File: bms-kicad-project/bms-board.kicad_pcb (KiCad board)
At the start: 2 copper layers, 49 parts, among them J1 S7B-XH-A, Q1 BSS308PE_H6327, Q2 BSS308PE_H6327, Q3 BSS308PE_H6327, Q5 BSS308PE_H6327, Q6 BSS308PE_H6327, Q7 BSS308PE_H6327, U1 LTC6804-2

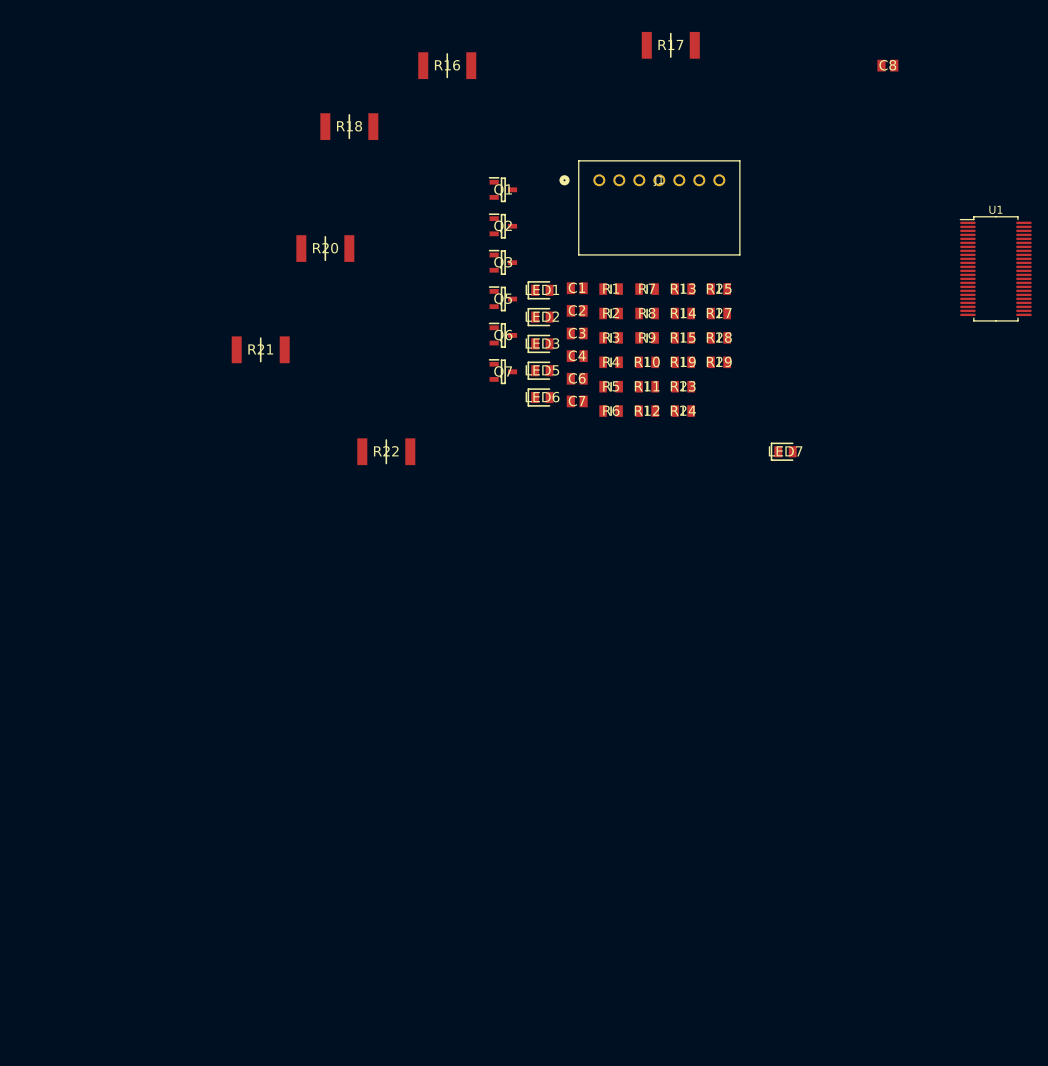
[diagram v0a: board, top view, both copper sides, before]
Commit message: Feature: Added schematic and symbols for 5V switching regulator (#16)
* feat: initial 5V-reg-and-edits branch commit

* feat: small to-do list edits

* feat: put filtering and balancing circuits into hierarchical format

* feat: forgot to commit smol change

* feat: Added SiC461 Schematic, Footprint, and 3D Model

* feat: Added all components listed in the spreadsheet, until Inductor L1

* feat: forgor the description

* feat: Added all symbols and 3D models. Also began working on Regulator Schematic.

* feat: Added more connections to the 5V Regulator schematic.

* feat: Added VFB connection in 5V Regulator Schematic

* feat: Added 220uf cap & modified 5V Reg Circuit

* feat: Added more to 5V Regulator Schematic

* feat: Changed all resistor symbols to be the standard KiCAD symbol, started improving schematic.

* feat: Forgot to save changes to schematic.

* feat: Just about completed 5V Regulator Schematic.

* feat: cosmetic changes to 5V reg schematic

* feat: Added comment boxes and fixed 5V Regulator Schematic.

* feat: just moved around and edited notes on the 5V reg schematic

* feat: re-ordered page numbers

* feat: Added snubber circuit to 5V Regulator schematic

* feat: Added 0OHM jumper between ULTRASONIC and VDD, added LED indicator for PGOOD

* feat: added buncha shit, refer to tasks 4 and 8

* feat: finished 5V reg circuit lgtm!

---------

Co-authored-by: cowman19 <matthewf9001@gmail.com>
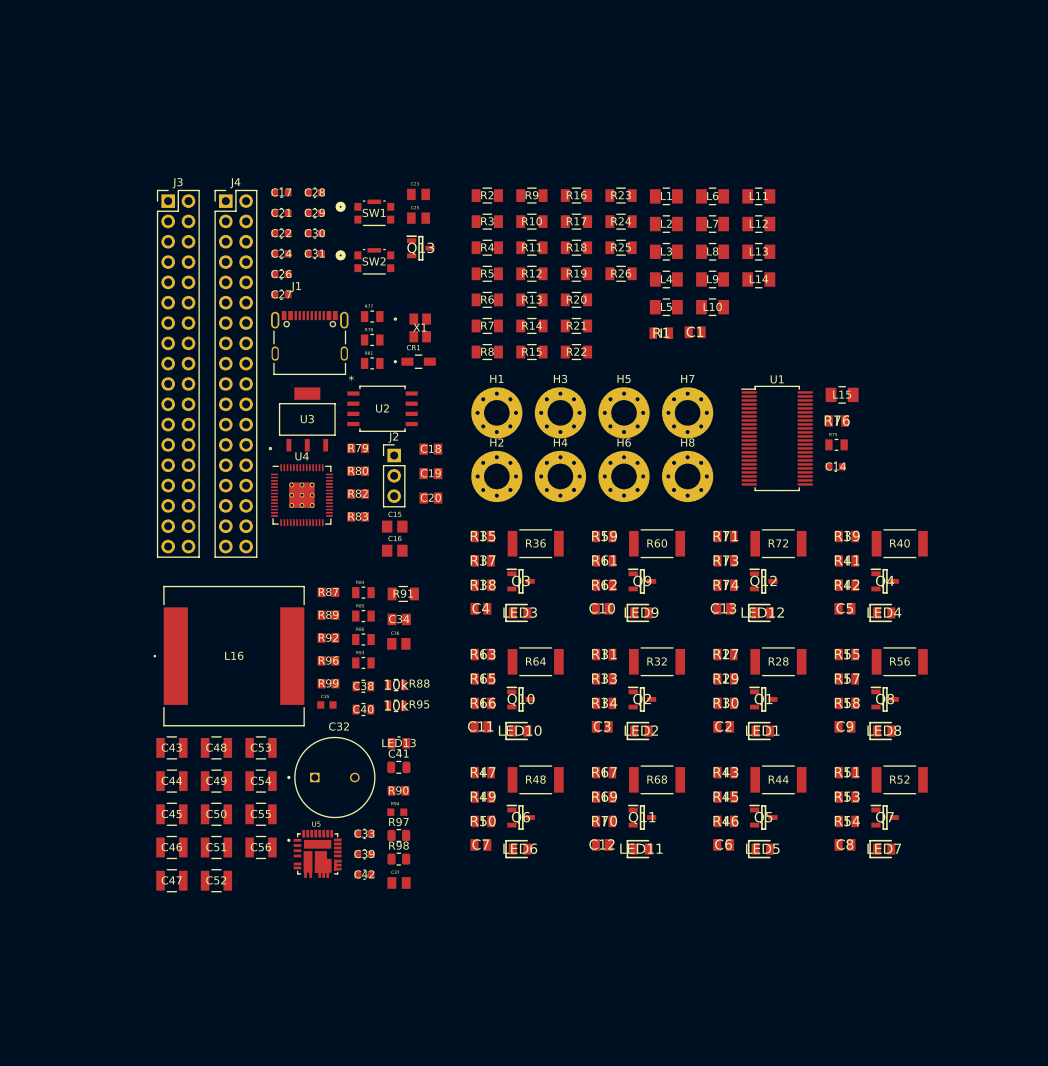
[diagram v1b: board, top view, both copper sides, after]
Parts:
- added C10: 10n, FixedWing:CAPC2012X95N, F.Cu at (141.3, 106.0)
- added C11: 10n, FixedWing:CAPC2012X95N, F.Cu at (126.1, 120.8)
- added C12: 10n, FixedWing:CAPC2012X95N, F.Cu at (141.3, 135.5)
- added C13: 10n, FixedWing:CAPC2012X95N, F.Cu at (156.5, 106.0)
- added C14: 0.1µ, FixedWing:CAP_GCJ-18_MUR, F.Cu at (170.5, 88.2)
- added C15: 15p, FixedWing:CAPC2012X70, F.Cu at (115.4, 95.7)
- added C16: 15p, FixedWing:CAPC2012X70, F.Cu at (115.4, 98.7)
- added C17: 0.1µ, FixedWing:CAP_GCJ-18_MUR, F.Cu at (101.2, 54.0)
- added C18: 10µ, FixedWing:CAP_CL21B106KOQNNNE_SAM, F.Cu at (119.9, 86.0)
- added C19: 10µ, FixedWing:CAP_CL21B106KOQNNNE_SAM, F.Cu at (119.9, 89.1)
- added C20: 10µ, FixedWing:CAP_CL21B106KOQNNNE_SAM, F.Cu at (119.9, 92.1)
- added C21: 0.1µ, FixedWing:CAP_GCJ-18_MUR, F.Cu at (101.2, 56.5)
- added C22: 0.1µ, FixedWing:CAP_GCJ-18_MUR, F.Cu at (101.2, 59.1)
- added C23: 1µ, FixedWing:CAPC2012X140N, F.Cu at (118.3, 54.2)
- added C24: 0.1µ, FixedWing:CAP_GCJ-18_MUR, F.Cu at (101.2, 61.6)
- added C25: 1µ, FixedWing:CAPC2012X140N, F.Cu at (118.3, 57.2)
- added C26: 0.1µ, FixedWing:CAP_GCJ-18_MUR, F.Cu at (101.2, 64.2)
- added C27: 0.1µ, FixedWing:CAP_GCJ-18_MUR, F.Cu at (101.2, 66.7)
- added C28: 0.1µ, FixedWing:CAP_GCJ-18_MUR, F.Cu at (105.4, 54.0)
- added C29: 0.1µ, FixedWing:CAP_GCJ-18_MUR, F.Cu at (105.4, 56.5)
- added C30: 0.1µ, FixedWing:CAP_GCJ-18_MUR, F.Cu at (105.4, 59.1)
- added C31: 0.1µ, FixedWing:CAP_GCJ-18_MUR, F.Cu at (105.4, 61.6)
- added C32: 220u, FixedWing:CAPPRD500W60D1000H2500, F.Cu at (107.9, 127.1)
- added C33: 0.1µ, FixedWing:CAP_GCJ-18_MUR, F.Cu at (111.6, 134.1)
- added C34: 560p, FixedWing:CAP_CC0805_YAG, F.Cu at (115.9, 107.3)
- added C35: 1u, FixedWing:CAPC1608X90N, F.Cu at (106.9, 118.0)
- added C36: 33n, FixedWing:CAPC2012X94N, F.Cu at (115.9, 110.4)
- added C37: 4.7u, FixedWing:CAPC2012X145N, F.Cu at (115.9, 140.3)
- added C38: 3.9n, FixedWing:G-21_MUR, F.Cu at (111.4, 115.7)
- added C39: 0.1µ, FixedWing:CAP_GCJ-18_MUR, F.Cu at (111.6, 136.7)
- added C40: 1.5n, FixedWing:G-21_MUR, F.Cu at (111.4, 118.6)
- added C41: C, Capacitor_SMD:C_0805_2012Metric, F.Cu at (115.9, 125.8)
- added C42: 0.1µ, FixedWing:CAP_GCJ-18_MUR, F.Cu at (111.6, 139.2)
- added C43: 47u, FixedWing:G-32_MUR, F.Cu at (87.5, 123.4)
- added C44: 47u, FixedWing:G-32_MUR, F.Cu at (87.5, 127.5)
- added C45: 47u, FixedWing:G-32_MUR, F.Cu at (87.5, 131.7)
- added C46: 47u, FixedWing:G-32_MUR, F.Cu at (87.5, 135.8)
- added C47: 47u, FixedWing:G-32_MUR, F.Cu at (87.5, 140.0)
- added C48: 47u, FixedWing:G-32_MUR, F.Cu at (93.1, 123.4)
- added C49: 47u, FixedWing:G-32_MUR, F.Cu at (93.1, 127.5)
- added C5: 10n, FixedWing:CAPC2012X95N, F.Cu at (171.6, 106.0)
- added C50: 47u, FixedWing:G-32_MUR, F.Cu at (93.1, 131.7)
- added C51: 47u, FixedWing:G-32_MUR, F.Cu at (93.1, 135.8)
- added C52: 47u, FixedWing:G-32_MUR, F.Cu at (93.1, 140.0)
- added C53: 47u, FixedWing:G-32_MUR, F.Cu at (98.6, 123.4)
- added C54: 47u, FixedWing:G-32_MUR, F.Cu at (98.6, 127.5)
- added C55: 47u, FixedWing:G-32_MUR, F.Cu at (98.6, 131.7)
- added C56: 47u, FixedWing:G-32_MUR, F.Cu at (98.6, 135.8)
- added C9: 10n, FixedWing:CAPC2012X95N, F.Cu at (171.6, 120.8)
- added CR1: MBR120VLSFT1G, FixedWing:DIOM3616X98N, F.Cu at (118.3, 75.1)
- added H1: MountingHole_Pad, MountingHole:MountingHole_3.2mm_M3_Pad_Via, F.Cu at (128.1, 81.5)
- added H2: MountingHole_Pad, MountingHole:MountingHole_3.2mm_M3_Pad_Via, F.Cu at (128.1, 89.5)
- added H3: MountingHole_Pad, MountingHole:MountingHole_3.2mm_M3_Pad_Via, F.Cu at (136.1, 81.5)
- added H4: MountingHole_Pad, MountingHole:MountingHole_3.2mm_M3_Pad_Via, F.Cu at (136.1, 89.5)
- added H5: MountingHole_Pad, MountingHole:MountingHole_3.2mm_M3_Pad_Via, F.Cu at (144.0, 81.5)
- added H6: MountingHole_Pad, MountingHole:MountingHole_3.2mm_M3_Pad_Via, F.Cu at (144.0, 89.5)
- added H7: MountingHole_Pad, MountingHole:MountingHole_3.2mm_M3_Pad_Via, F.Cu at (152.0, 81.5)
- added H8: MountingHole_Pad, MountingHole:MountingHole_3.2mm_M3_Pad_Via, F.Cu at (152.0, 89.5)
- added J2: DEBUG, Connector_PinHeader_2.54mm:PinHeader_1x03_P2.54mm_Vertical, F.Cu at (115.3, 86.8)
- added J3: Conn_02x18_Odd_Even, Connector_PinHeader_2.54mm:PinHeader_2x18_P2.54mm_Vertical, F.Cu at (87.0, 55.0)
- added J4: Conn_02x18_Odd_Even, Connector_PinHeader_2.54mm:PinHeader_2x18_P2.54mm_Vertical, F.Cu at (94.2, 55.0)
- added L1: 600Ω, FixedWing:IND_BLM31PG391SN1L_MUR, F.Cu at (149.3, 54.4)
- added L10: 600Ω, FixedWing:IND_BLM31PG391SN1L_MUR, F.Cu at (155.1, 68.3)
- added L11: 600Ω, FixedWing:IND_BLM31PG391SN1L_MUR, F.Cu at (160.9, 54.4)
- added L12: 600Ω, FixedWing:IND_BLM31PG391SN1L_MUR, F.Cu at (160.9, 57.9)
- added L13: 600Ω, FixedWing:IND_BLM31PG391SN1L_MUR, F.Cu at (160.9, 61.4)
- added L14: 600Ω, FixedWing:IND_BLM31PG391SN1L_MUR, F.Cu at (160.9, 64.8)
- added L15: 600Ω, FixedWing:IND_BLM31PG391SN1L_MUR, F.Cu at (171.3, 79.3)
- added L16: 5.6u, FixedWing:IND_IHLP-6767GZ_VIS, F.Cu at (95.3, 111.9)
- added L2: 600Ω, FixedWing:IND_BLM31PG391SN1L_MUR, F.Cu at (149.3, 57.9)
- added L3: 600Ω, FixedWing:IND_BLM31PG391SN1L_MUR, F.Cu at (149.3, 61.4)
- added L4: 600Ω, FixedWing:IND_BLM31PG391SN1L_MUR, F.Cu at (149.3, 64.8)
- added L5: 600Ω, FixedWing:IND_BLM31PG391SN1L_MUR, F.Cu at (149.3, 68.3)
- added L6: 600Ω, FixedWing:IND_BLM31PG391SN1L_MUR, F.Cu at (155.1, 54.4)
- added L7: 600Ω, FixedWing:IND_BLM31PG391SN1L_MUR, F.Cu at (155.1, 57.9)
- added L8: 600Ω, FixedWing:IND_BLM31PG391SN1L_MUR, F.Cu at (155.1, 61.4)
- added L9: 600Ω, FixedWing:IND_BLM31PG391SN1L_MUR, F.Cu at (155.1, 64.8)
- added LED10: LTST-C170KRKT, FixedWing:LEDC2012X120N, F.Cu at (131.0, 121.3)
- added LED11: LTST-C170KRKT, FixedWing:LEDC2012X120N, F.Cu at (146.2, 136.0)
- added LED12: LTST-C170KRKT, FixedWing:LEDC2012X120N, F.Cu at (161.4, 106.5)
- added LED13: LTST-C170KGKT, FixedWing:LED_LTST-C170KGKT_LTO, F.Cu at (115.9, 122.8)
- added LED4: LTST-C170KRKT, FixedWing:LEDC2012X120N, F.Cu at (176.5, 106.5)
- added LED8: LTST-C170KRKT, FixedWing:LEDC2012X120N, F.Cu at (176.5, 121.3)
- added LED9: LTST-C170KRKT, FixedWing:LEDC2012X120N, F.Cu at (146.2, 106.5)
- added Q10: BSS308PE_H6327, FixedWing:SOT95P260X110-3N, F.Cu at (131.1, 117.3)
- added Q11: BSS308PE_H6327, FixedWing:SOT95P260X110-3N, F.Cu at (146.3, 132.1)
- added Q12: BSS308PE_H6327, FixedWing:SOT95P260X110-3N, F.Cu at (161.5, 102.6)
- added Q13: BSS308PE_H6327, FixedWing:SOT95P260X110-3N, F.Cu at (118.6, 60.9)
- added Q4: BSS308PE_H6327, FixedWing:SOT95P260X110-3N, F.Cu at (176.7, 102.6)
- added Q8: BSS308PE_H6327, FixedWing:SOT95P260X110-3N, F.Cu at (176.7, 117.3)
- added Q9: BSS308PE_H6327, FixedWing:SOT95P260X110-3N, F.Cu at (146.3, 102.6)
- added R26: 0, FixedWing:RC1206N_YAG, F.Cu at (143.6, 64.1)
- added R30: 3.3k, FixedWing:RESC2012X50N, F.Cu at (156.7, 117.8)
- added R31: 475, FixedWing:RESC2012X50N, F.Cu at (141.6, 111.7)
- added R32: 33, FixedWing:RC2512N_VIS, F.Cu at (148.1, 112.6)
- added R33: 100, FixedWing:RESC2012X50N, F.Cu at (141.6, 114.8)
- added R34: 3.3k, FixedWing:RESC2012X50N, F.Cu at (141.6, 117.8)
- added R35: 475, FixedWing:RESC2012X50N, F.Cu at (126.4, 97.0)
- added R36: 33, FixedWing:RC2512N_VIS, F.Cu at (133.0, 97.9)
- added R37: 100, FixedWing:RESC2012X50N, F.Cu at (126.4, 100.0)
- added R38: 3.3k, FixedWing:RESC2012X50N, F.Cu at (126.4, 103.0)
- added R39: 475, FixedWing:RESC2012X50N, F.Cu at (171.9, 97.0)
- added R40: 33, FixedWing:RC2512N_VIS, F.Cu at (178.5, 97.9)
- added R41: 100, FixedWing:RESC2012X50N, F.Cu at (171.9, 100.0)
- added R42: 3.3k, FixedWing:RESC2012X50N, F.Cu at (171.9, 103.0)
- added R43: 475, FixedWing:RESC2012X50N, F.Cu at (156.7, 126.5)
- added R44: 33, FixedWing:RC2512N_VIS, F.Cu at (163.3, 127.4)
- added R45: 100, FixedWing:RESC2012X50N, F.Cu at (156.7, 129.5)
- added R46: 3.3k, FixedWing:RESC2012X50N, F.Cu at (156.7, 132.6)
- added R47: 475, FixedWing:RESC2012X50N, F.Cu at (126.4, 126.5)
- added R48: 33, FixedWing:RC2512N_VIS, F.Cu at (133.0, 127.4)
- added R49: 100, FixedWing:RESC2012X50N, F.Cu at (126.4, 129.5)
- added R50: 3.3k, FixedWing:RESC2012X50N, F.Cu at (126.4, 132.6)
- added R51: 475, FixedWing:RESC2012X50N, F.Cu at (171.9, 126.5)
- added R52: 33, FixedWing:RC2512N_VIS, F.Cu at (178.5, 127.4)
- added R53: 100, FixedWing:RESC2012X50N, F.Cu at (171.9, 129.5)
- added R54: 3.3k, FixedWing:RESC2012X50N, F.Cu at (171.9, 132.6)
- added R55: 475, FixedWing:RESC2012X50N, F.Cu at (171.9, 111.7)
- added R56: 33, FixedWing:RC2512N_VIS, F.Cu at (178.5, 112.6)
- added R57: 100, FixedWing:RESC2012X50N, F.Cu at (171.9, 114.8)
- added R58: 3.3k, FixedWing:RESC2012X50N, F.Cu at (171.9, 117.8)
- added R59: 475, FixedWing:RESC2012X50N, F.Cu at (141.6, 97.0)
- added R60: 33, FixedWing:RC2512N_VIS, F.Cu at (148.1, 97.9)
- added R61: 100, FixedWing:RESC2012X50N, F.Cu at (141.6, 100.0)
- added R62: 3.3k, FixedWing:RESC2012X50N, F.Cu at (141.6, 103.0)
- added R63: 475, FixedWing:RESC2012X50N, F.Cu at (126.4, 111.7)
- added R64: 33, FixedWing:RC2512N_VIS, F.Cu at (133.0, 112.6)
- added R65: 100, FixedWing:RESC2012X50N, F.Cu at (126.4, 114.8)
- added R66: 3.3k, FixedWing:RESC2012X50N, F.Cu at (126.4, 117.8)
- added R67: 475, FixedWing:RESC2012X50N, F.Cu at (141.6, 126.5)
- added R68: 33, FixedWing:RC2512N_VIS, F.Cu at (148.1, 127.4)
- added R69: 100, FixedWing:RESC2012X50N, F.Cu at (141.6, 129.5)
- added R70: 3.3k, FixedWing:RESC2012X50N, F.Cu at (141.6, 132.6)
- added R71: 475, FixedWing:RESC2012X50N, F.Cu at (156.7, 97.0)
- added R72: 33, FixedWing:RC2512N_VIS, F.Cu at (163.3, 97.9)
- added R73: 100, FixedWing:RESC2012X50N, F.Cu at (156.7, 100.0)
- added R74: 3.3k, FixedWing:RESC2012X50N, F.Cu at (156.7, 103.0)
- added R75: 5.6k, FixedWing:RESC2012X60N, F.Cu at (170.6, 85.5)
- added R76: 100, FixedWing:RESC2012X50N, F.Cu at (170.6, 82.5)
- added R77: 5.6k, FixedWing:RESC2012X60N, F.Cu at (112.5, 69.5)
- added R78: 5.6k, FixedWing:RESC2012X60N, F.Cu at (112.5, 72.4)
- added R79: 1k, FixedWing:RC0805N_YAG, F.Cu at (110.8, 85.9)
- added R80: 1k, FixedWing:RC0805N_YAG, F.Cu at (110.8, 88.8)
- added R81: 5.6k, FixedWing:RESC2012X60N, F.Cu at (112.5, 75.3)
- added R82: 27, FixedWing:RC0805N_YAG, F.Cu at (110.8, 91.6)
- added R83: 27, FixedWing:RC0805N_YAG, F.Cu at (110.8, 94.5)
- added R84: 562k, FixedWing:RESC2012X60N, F.Cu at (111.4, 104.0)
- added R85: 100k, FixedWing:RESC2012X60N, F.Cu at (111.4, 106.9)
- added R86: 100k, FixedWing:RESC2012X60N, F.Cu at (111.4, 109.8)
- added R87: 523k, FixedWing:RC0805N_YAG, F.Cu at (107.1, 103.9)
- added R88: 10k, FixedWing:KOA_Speer-RK73H2A-0-0-MFG, F.Cu at (115.5, 115.5)
- added R89: 1k, FixedWing:RC0805N_YAG, F.Cu at (107.1, 106.8)
- added R90: 41.2, FixedWing:RC0805N_VIS, F.Cu at (115.8, 128.7)
- added R91: 0, FixedWing:RC1206N_YAG, F.Cu at (116.4, 104.1)
- added R92: 1k, FixedWing:RC0805N_YAG, F.Cu at (107.1, 109.6)
- added R93: 93.1k, FixedWing:RESC2012X60N, F.Cu at (111.4, 112.8)
- added R94: 3.3, FixedWing:RESC1608X55N, F.Cu at (115.7, 131.4)
- added R95: 10k, FixedWing:KOA_Speer-RK73H2A-0-0-MFG, F.Cu at (115.5, 118.1)
- added R96: 11.5k, FixedWing:RC0805N_YAG, F.Cu at (107.1, 112.5)
- added R97: R, Resistor_SMD:R_0805_2012Metric, F.Cu at (115.9, 134.3)
- added R98: R, Resistor_SMD:R_0805_2012Metric, F.Cu at (115.9, 137.3)
- added R99: 56.2k, FixedWing:RC0805N_YAG, F.Cu at (107.1, 115.3)
- added SW1: KMR223G LFG, FixedWing:KMR2_G_CNK, F.Cu at (112.8, 56.5)
- added SW2: KMR223G LFG, FixedWing:KMR2_G_CNK, F.Cu at (112.8, 62.6)
- added U2: W25Q128JVSIQ TR, FixedWing:SOIC_208MIL_WIN, F.Cu at (113.8, 81.0)
- added U3: NCP1117ST33T3G, FixedWing:SOT223-3_ONS, F.Cu at (104.4, 82.3)
- added U4: RP2040, FixedWing:RP2040-QFN-56, F.Cu at (103.8, 91.8)
- added U5: SIC461ED-T1-GE3, FixedWing:CONV_SIC461ED-T1-GE3, F.Cu at (105.7, 136.6)
- added X1: ABM8-272-T3, FixedWing:ABM8-272-T3_ABR, F.Cu at (118.5, 70.9)
- C1, C2, C3, C4, C6, C7, C8: value 10nF -> 10n
- J1: value S7B-XH-A -> 12402012E212A; footprint FixedWing:CONN_S7B-XH-A_JST -> FixedWing:AMPHENOL_12402012E212A
- R1: value 100Ω -> 100
- R10, R11, R13, R14, R15, R9: value 475Ω -> 0; footprint FixedWing:RESC2012X50N -> FixedWing:RC1206N_YAG
- R12, R19, R2, R3, R4, R5, R6, R7, R8: value 100Ω -> 0; footprint FixedWing:RESC2012X50N -> FixedWing:RC1206N_YAG
- R16, R17, R18, R20, R21, R22: value 33Ω -> 0; footprint FixedWing:RESC6332X70N -> FixedWing:RC1206N_YAG
- R23, R24, R25: value 3k3Ω -> 0; footprint FixedWing:RESC2012X50N -> FixedWing:RC1206N_YAG
- R27: value 3k3Ω -> 475
- R28: value 3k3Ω -> 33; footprint FixedWing:RESC2012X50N -> FixedWing:RC2512N_VIS
- R29: value 3k3Ω -> 100
- U1: footprint Package_SO:SSOP-48_5.3x12.8mm_P0.5mm -> FixedWing:SSOP-48_5.3x12.8mm_P0.5mm
- moved C8 97.6 mm to (171.6, 135.5)
- moved Q7 73.4 mm to (176.7, 132.1)
- moved Q5 72.5 mm to (161.5, 132.1)
- moved Q1 71.5 mm to (161.5, 117.3)
- moved LED5 65.8 mm to (161.4, 136.0)
- moved Q2 61.7 mm to (146.3, 117.3)
- moved LED1 61.6 mm to (161.4, 121.3)
- moved C6 61.1 mm to (156.5, 135.5)
- moved Q6 60.3 mm to (131.1, 132.1)
- moved C7 56.7 mm to (126.1, 135.5)
- moved LED6 56.5 mm to (131.0, 136.0)
- moved C2 55.1 mm to (156.5, 120.8)
- moved LED2 53.2 mm to (146.2, 121.3)
- moved LED7 51.2 mm to (176.5, 136.0)
- moved C3 49.3 mm to (141.3, 120.8)
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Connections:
- C1 pad 1: C0 -> /Cell Filtering and Balancing/Filter and Balance Cell 1/C(n-1)
- C2 pad 1: C1 -> /Cell Filtering and Balancing/Filter and Balance Cell 1/C(n)
- C2 pad 2: C0 -> /Cell Filtering and Balancing/Filter and Balance Cell 1/C(n-1)
- C3 pad 1: C2 -> /Cell Filtering and Balancing/Filter and Balance Cell 2/C(n)
- C3 pad 2: C1 -> /Cell Filtering and Balancing/Filter and Balance Cell 1/C(n)
- C4 pad 1: C3 -> /Cell Filtering and Balancing/Filter and Balance Cell 3/C(n)
- C4 pad 2: C2 -> /Cell Filtering and Balancing/Filter and Balance Cell 2/C(n)
- C6 pad 1: C7 -> /Cell Filtering and Balancing/Filter and Balance Cell 5/C(n)
- C6 pad 2: C3 -> /Cell Filtering and Balancing/Filter and Balance Cell 4/C(n)
- C7 pad 1: C8 -> /Cell Filtering and Balancing/Filter and Balance Cell 6/C(n)
- C7 pad 2: C7 -> /Cell Filtering and Balancing/Filter and Balance Cell 5/C(n)
- C8 pad 1: C9 -> /Cell Filtering and Balancing/Filter and Balance Cell 7/C(n)
- C8 pad 2: C8 -> /Cell Filtering and Balancing/Filter and Balance Cell 6/C(n)
- Q1 pad 2: Net-(Q1-S) -> /Cell Filtering and Balancing/Filter and Balance Cell 1/BATT(n)
- Q2 pad 2: Net-(Q2-S) -> /Cell Filtering and Balancing/Filter and Balance Cell 2/BATT(n)
- Q3 pad 2: Net-(Q3-S) -> /Cell Filtering and Balancing/Filter and Balance Cell 3/BATT(n)
- Q5 pad 2: Net-(Q5-S) -> /Cell Filtering and Balancing/Filter and Balance Cell 5/BATT(n)
- Q6 pad 2: Net-(Q6-S) -> /Cell Filtering and Balancing/Filter and Balance Cell 6/BATT(n)
- Q7 pad 2: Net-(Q7-S) -> /Cell Filtering and Balancing/Filter and Balance Cell 7/BATT(n)
- R1 pad 1: GND -> /Cell Filtering and Balancing/Filter and Balance Cell 12/BATT(n)
- R1 pad 2: C0 -> unconnected-(R1-Pad2)
- R10 pad 1: Net-(Q1-S) -> /Cell Filtering and Balancing/Filter and Balance Cell 4/C(n)
- R10 pad 2: Net-(LED2-K) -> /Battery Stack Monitor/C4
- R11 pad 1: Net-(Q2-S) -> /Cell Filtering and Balancing/Filter and Balance Cell 3/C(n)
- R11 pad 2: Net-(LED3-K) -> /Battery Stack Monitor/C3
- R12 pad 1: Net-(Q7-S) -> /Cell Filtering and Balancing/Filter and Balance Cell 2/C(n)
- R12 pad 2: C12 -> /Battery Stack Monitor/C2
- R13 pad 1: Net-(Q3-S) -> /Cell Filtering and Balancing/Filter and Balance Cell 1/C(n)
- R13 pad 2: Net-(LED5-K) -> /Battery Stack Monitor/C1
- R14 pad 1: Net-(Q5-S) -> /Cell Filtering and Balancing/Filter and Balance Cell 1/C(n-1)
- R14 pad 2: Net-(LED6-K) -> /Battery Stack Monitor/C0
- R15 pad 1: Net-(Q6-S) -> /Cell Filtering and Balancing/Filter and Balance Cell 12/S(n)
- R15 pad 2: Net-(LED7-K) -> /Battery Stack Monitor/S12
- R16 pad 1: GND -> /Cell Filtering and Balancing/Filter and Balance Cell 11/S(n)
- R16 pad 2: Net-(LED1-A) -> /Battery Stack Monitor/S11
- R17 pad 1: Net-(Q1-S) -> /Cell Filtering and Balancing/Filter and Balance Cell 10/S(n)
- R17 pad 2: Net-(LED2-A) -> /Battery Stack Monitor/S10
- R18 pad 1: Net-(Q2-S) -> /Cell Filtering and Balancing/Filter and Balance Cell 9/S(n)
- R18 pad 2: Net-(LED3-A) -> /Battery Stack Monitor/S9
- R19 pad 1: Net-(Q7-S) -> /Cell Filtering and Balancing/Filter and Balance Cell 8/S(n)
- R19 pad 2: VIN_MONITOR -> /Battery Stack Monitor/S8
- R2 pad 1: Net-(Q1-S) -> /Cell Filtering and Balancing/Filter and Balance Cell 12/C(n)
- R2 pad 2: C1 -> /Battery Stack Monitor/C12
- R20 pad 1: Net-(Q3-S) -> /Cell Filtering and Balancing/Filter and Balance Cell 7/S(n)
- R20 pad 2: Net-(LED5-A) -> /Battery Stack Monitor/S7
- R21 pad 1: Net-(Q5-S) -> /Cell Filtering and Balancing/Filter and Balance Cell 6/S(n)
- R21 pad 2: Net-(LED6-A) -> /Battery Stack Monitor/S6
- R22 pad 1: Net-(Q6-S) -> /Cell Filtering and Balancing/Filter and Balance Cell 5/S(n)
- R22 pad 2: Net-(LED7-A) -> /Battery Stack Monitor/S5
- R23 pad 1: S1 -> /Cell Filtering and Balancing/Filter and Balance Cell 4/S(n)
- R23 pad 2: Net-(Q1-G) -> /Battery Stack Monitor/S4
- R24 pad 1: S2 -> /Cell Filtering and Balancing/Filter and Balance Cell 3/S(n)
- R24 pad 2: Net-(Q2-G) -> /Battery Stack Monitor/S3
- R25 pad 1: S3 -> /Cell Filtering and Balancing/Filter and Balance Cell 2/S(n)
- R25 pad 2: Net-(Q3-G) -> /Battery Stack Monitor/S2
- R27 pad 1: S7 -> /Cell Filtering and Balancing/Filter and Balance Cell 1/BATT(n-1)
- R27 pad 2: Net-(Q5-G) -> Net-(LED1-K)
- R28 pad 1: S8 -> /Cell Filtering and Balancing/Filter and Balance Cell 1/BATT(n-1)
- R28 pad 2: Net-(Q6-G) -> Net-(LED1-A)
- R29 pad 1: S9 -> /Cell Filtering and Balancing/Filter and Balance Cell 1/BATT(n-1)
- R29 pad 2: Net-(Q7-G) -> /Cell Filtering and Balancing/Filter and Balance Cell 1/C(n-1)
- R3 pad 1: Net-(Q2-S) -> /Cell Filtering and Balancing/Filter and Balance Cell 11/C(n)
- R3 pad 2: C2 -> /Battery Stack Monitor/C11
- R4 pad 1: Net-(Q3-S) -> /Cell Filtering and Balancing/Filter and Balance Cell 10/C(n)
- R4 pad 2: C3 -> /Battery Stack Monitor/C10
- R5 pad 1: Net-(Q3-S) -> /Cell Filtering and Balancing/Filter and Balance Cell 10/C(n-1)
- R5 pad 2: C6 -> /Battery Stack Monitor/C9
- R6 pad 1: Net-(Q5-S) -> /Cell Filtering and Balancing/Filter and Balance Cell 8/C(n)
- R6 pad 2: C7 -> /Battery Stack Monitor/C8
- R7 pad 1: Net-(Q6-S) -> /Cell Filtering and Balancing/Filter and Balance Cell 7/C(n)
- R7 pad 2: C8 -> /Battery Stack Monitor/C7
- R8 pad 1: Net-(Q7-S) -> /Cell Filtering and Balancing/Filter and Balance Cell 6/C(n)
- R8 pad 2: C9 -> /Battery Stack Monitor/C6
- R9 pad 1: GND -> /Cell Filtering and Balancing/Filter and Balance Cell 5/C(n)
- R9 pad 2: Net-(LED1-K) -> /Battery Stack Monitor/C5
- U1 pad 1: VIN_MONITOR -> Net-(U1-V+)
- U1 pad 10: C8 -> /Battery Stack Monitor/C8
- U1 pad 11: S8 -> /Battery Stack Monitor/S8
- U1 pad 12: C7 -> /Battery Stack Monitor/C7
- U1 pad 13: S7 -> /Battery Stack Monitor/S7
- U1 pad 14: C6 -> /Battery Stack Monitor/C6
- U1 pad 15: unconnected-(U1-S6-Pad15) -> /Battery Stack Monitor/S6
- U1 pad 16: C6 -> /Battery Stack Monitor/C5
- U1 pad 17: unconnected-(U1-S5-Pad17) -> /Battery Stack Monitor/S5
- U1 pad 18: C6 -> /Battery Stack Monitor/C4
- U1 pad 19: unconnected-(U1-S4-Pad19) -> /Battery Stack Monitor/S4
- U1 pad 2: C12 -> /Battery Stack Monitor/C12
- U1 pad 20: C3 -> /Battery Stack Monitor/C3
- U1 pad 21: S3 -> /Battery Stack Monitor/S3
- U1 pad 22: C2 -> /Battery Stack Monitor/C2
- U1 pad 23: S2 -> /Battery Stack Monitor/S2
- U1 pad 24: C1 -> /Battery Stack Monitor/C1
- U1 pad 25: S1 -> /Battery Stack Monitor/S1
- U1 pad 26: C0 -> /Battery Stack Monitor/C0
- U1 pad 3: unconnected-(U1-S12-Pad3) -> /Battery Stack Monitor/S12
- U1 pad 37: unconnected-(U1-VREG-Pad37) -> +5V
- U1 pad 4: C12 -> /Battery Stack Monitor/C11
- U1 pad 40: unconnected-(U1-ISOMD-Pad40) -> GND
- U1 pad 41: unconnected-(U1-CSB(IMA)-Pad41) -> /RP2040 Microcontroller/GPIO1
- U1 pad 42: unconnected-(U1-SCK(IPA)-Pad42) -> /RP2040 Microcontroller/GPIO2
- U1 pad 43: unconnected-(U1-SDI(ICMP)-Pad43) -> /RP2040 Microcontroller/GPIO3
- U1 pad 44: unconnected-(U1-SDO(IBIAS)-Pad44) -> /RP2040 Microcontroller/GPIO0
- U1 pad 5: unconnected-(U1-S11-Pad5) -> /Battery Stack Monitor/S11
- U1 pad 6: C12 -> /Battery Stack Monitor/C10
- U1 pad 7: unconnected-(U1-S10-Pad7) -> /Battery Stack Monitor/S10
- U1 pad 8: C9 -> /Battery Stack Monitor/C9
- U1 pad 9: S9 -> /Battery Stack Monitor/S9
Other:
- copper layers 2 -> 4

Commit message: feat: figured out battery stack monitor V+ biasing. Refer to task 5 on the punchlist for more details.
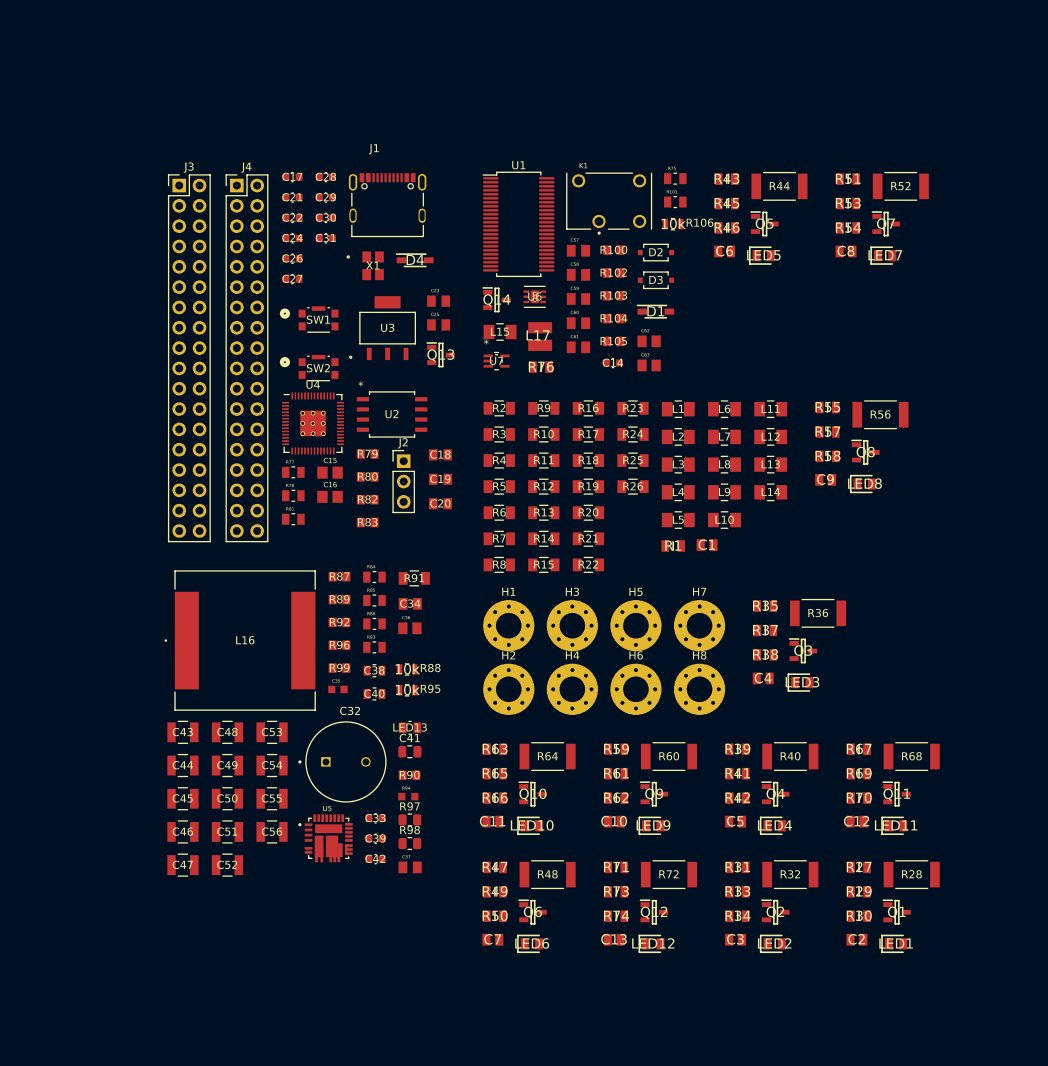
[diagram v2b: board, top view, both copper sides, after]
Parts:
- removed CR1: MBR120VLSFT1G, FixedWing:DIOM3616X98N
- added C57: 4.7u, FixedWing:CAPC2012X145N, F.Cu at (138.3, 61.2)
- added C58: 4.7u, FixedWing:CAPC2012X145N, F.Cu at (138.3, 64.3)
- added C59: 4.7u, FixedWing:CAPC2012X145N, F.Cu at (138.3, 67.3)
- added C60: 4.7u, FixedWing:CAPC2012X145N, F.Cu at (138.3, 70.3)
- added C61: 4.7u, FixedWing:CAPC2012X145N, F.Cu at (138.3, 73.3)
- added C62: 33n, FixedWing:CAPC2012X94N, F.Cu at (147.1, 72.6)
- added C63: 33n, FixedWing:CAPC2012X94N, F.Cu at (147.1, 75.6)
- added D1: B130LAW-7-F, FixedWing:SOD3716X145N, F.Cu at (148.0, 68.8)
- added D2: CMHD4448, FixedWing:CR_SOD-123F_CNS, F.Cu at (148.0, 61.5)
- added D3: CMHD4448, FixedWing:CR_SOD-123F_CNS, F.Cu at (148.0, 64.9)
- added D4: B130LAW-7-F, FixedWing:SOD3716X145N, F.Cu at (117.9, 62.4)
- added K1: G6L-1P_DC5, FixedWing:RELAY_G6L-1P_DC5, F.Cu at (142.2, 55.0)
- added L17: SDR0302-120ML, FixedWing:SDR0302-471KL, F.Cu at (133.5, 72.0)
- added Q14: BSS308PE_H6327, FixedWing:SOT95P260X110-3N, F.Cu at (128.1, 67.4)
- added R100: 11k5, FixedWing:RC0805N_YAG, F.Cu at (142.7, 61.2)
- added R101: 100k, FixedWing:RESC2012X60N, F.Cu at (150.4, 55.2)
- added R102: 56k2, FixedWing:RC0805N_YAG, F.Cu at (142.7, 64.0)
- added R103: 33k2, FixedWing:RC0805N_YAG, F.Cu at (142.7, 66.9)
- added R104: 33k2, FixedWing:RC0805N_YAG, F.Cu at (142.7, 69.7)
- added R105: 56k2, FixedWing:RC0805N_YAG, F.Cu at (142.7, 72.6)
- added R106: 10k, FixedWing:KOA_Speer-RK73H2A-0-0-MFG, F.Cu at (150.1, 57.9)
- added U6: TPS61170DRVR, FixedWing:DRV6_1P6X1, F.Cu at (132.9, 67.0)
- added U7: SN74LVC1G17DCKR, FixedWing:DCK5, F.Cu at (128.1, 75.0)
- moved Q5 74.2 mm to (161.6, 57.9)
- moved Q7 74.2 mm to (176.8, 57.9)
- moved R45 74.2 mm to (156.9, 55.3)
- moved R53 74.2 mm to (172.0, 55.3)
- moved LED5 74.2 mm to (161.5, 61.8)
- moved LED7 74.2 mm to (176.7, 61.8)
- moved R43 74.2 mm to (156.9, 52.3)
- moved R44 74.2 mm to (163.4, 53.2)
- moved R51 74.2 mm to (172.0, 52.3)
- moved R52 74.2 mm to (178.6, 53.2)
- moved C6 74.2 mm to (156.6, 61.3)
- moved C8 74.2 mm to (171.8, 61.3)
- moved R46 74.2 mm to (156.9, 58.4)
- moved R54 74.2 mm to (172.0, 58.4)
- moved C13 43.6 mm to (142.8, 147.4)
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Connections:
- L15 pad 1: +BATT -> Net-(L15-Pad1)
- L15 pad 2: Net-(L15-Pad2) -> Net-(D2-Pad1)
- R1 pad 2: unconnected-(R1-Pad2) -> /Cell Filtering and Balancing/Filter and Balance Cell 12/C(n)
- R76 pad 2: Net-(L15-Pad2) -> Net-(L15-Pad1)
- U4 pad 1: unconnected-(U4-IOVDD-Pad1) -> +3V3
- U4 pad 10: unconnected-(U4-IOVDD-Pad10) -> +3V3
- U4 pad 22: unconnected-(U4-IOVDD-Pad22) -> +3V3
- U4 pad 23: unconnected-(U4-DVDD-Pad23) -> +1V1
- U4 pad 33: unconnected-(U4-IOVDD-Pad33) -> +3V3
- U4 pad 42: unconnected-(U4-IOVDD-Pad42) -> +3V3
- U4 pad 43: unconnected-(U4-ADC_AVDD-Pad43) -> +3V3
- U4 pad 48: unconnected-(U4-USB_VDD-Pad48) -> +3V3
- U4 pad 49: unconnected-(U4-IOVDD-Pad49) -> +3V3
- U4 pad 50: unconnected-(U4-DVDD-Pad50) -> +1V1
